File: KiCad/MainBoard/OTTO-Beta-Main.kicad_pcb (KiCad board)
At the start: 4 copper layers, 288.5 x 95 mm, 333 parts, among them J1 Conn_ARM_JTAG_SWD_10, J2 Conn_02x04, J201 Raspberry Pi Connector, J206 Conn_02x06, J207 Conn_02x03, J3 Conn_02x05, J4 Conn_02x05, J5 Conn_02x05, J6 Conn_02x05, J7 Conn_01x20, J9 Conn_01x03, Q1 AO4407A, Q2 2N7002, SW1 ALPS SKHC, SW10 ALPS SKHC, SW11 ALPS SKHC, SW12 ALPS SKHC, SW13 ALPS SKHC, SW14 ALPS SKHC, SW15 ALPS SKHC, SW16 ALPS SKHC, SW17 ALPS SKHC, SW18 ALPS SKHC, SW19 ALPS SKHC, SW2 ALPS SKHC, SW20 ALPS SKHC, SW201 5.2x5.2x1.5mm, SW202 SW_DIP_x02, SW21 ALPS SKHC, SW22 ALPS SKHC, SW23 ALPS SKHC, SW24 ALPS SKHC, SW25 ALPS SKHC, SW26 ALPS SKHC, SW27 6x6x13mm, SW28 6x6x13mm, SW29 6x6x13mm, SW3 ALPS SKHC, SW30 6x6x13mm, SW31 6x6x13mm, SW32 6x6x13mm, SW33 6x6x13mm, SW34 6x6x13mm, SW35 6x6x13mm, SW36 6x6x13mm, SW37 6x6x13mm, SW38 6x6x13mm, SW39 6x6x13mm, SW4 ALPS SKHC, SW40 6x6x13mm, SW41 6x6x13mm, SW42 6x6x13mm, SW43 6x6x13mm, SW44 6x6x13mm, SW45 6x6x13mm, SW46 6x6x13mm, SW47 6x6x13mm, SW48 SW_DIP_x02, SW49 SW_DPDT_x2, SW5 ALPS SKHC, SW50 6x6x13mm, SW51 6x6x13mm, SW52 6x6x13mm, SW53 6x6x13mm, SW54 6x6x13mm, SW55 6x6x13mm, SW56 6x6x13mm, SW6 ALPS SKHC, SW7 ALPS SKHC, SW8 ALPS SKHC, SW9 ALPS SKHC, U1 TPS5430DDA, U2 TPS54331DR, U201 6N137, U202 STM32F407VGTx, U204 SRV05-4, U205 SN74HC14, U207 WM8731, U208 AMS1117-3.3, U5 TPS22918_SOT23-6_A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

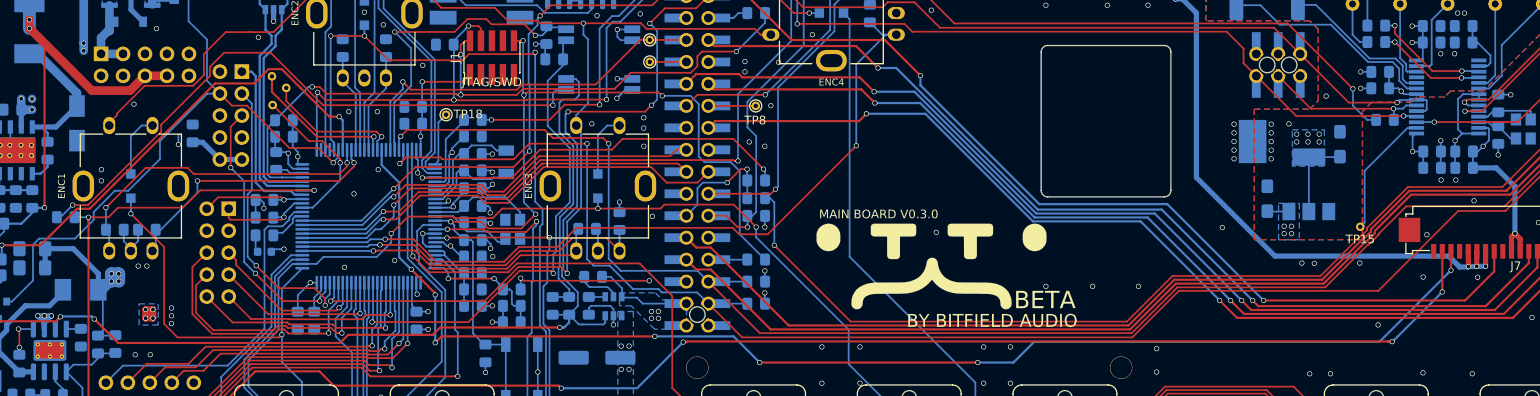
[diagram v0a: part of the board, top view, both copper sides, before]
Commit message: LEDs on PI power on main board
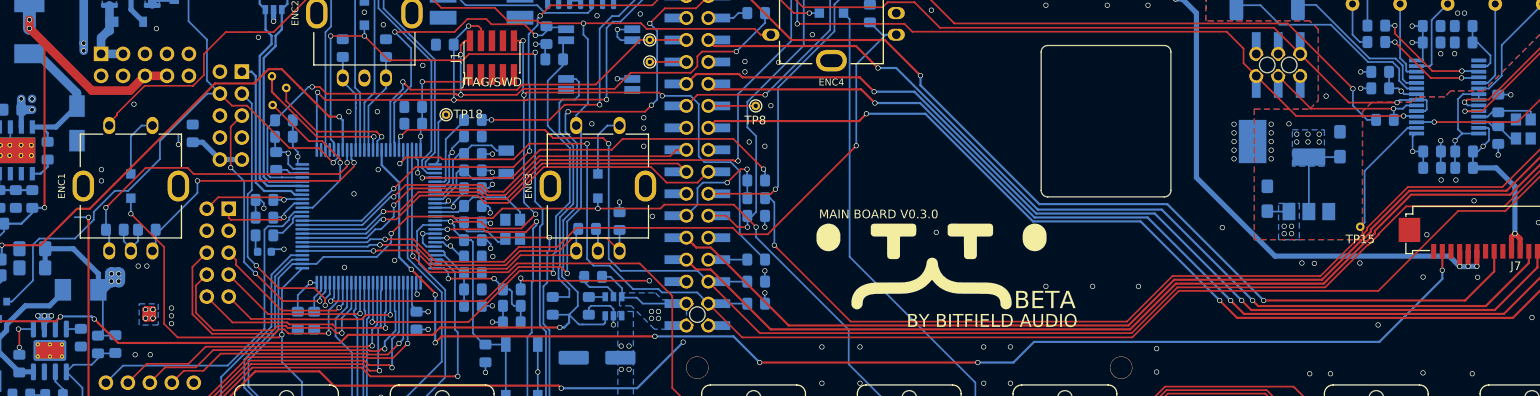
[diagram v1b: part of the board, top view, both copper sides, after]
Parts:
- removed R31, R32: 10k, Resistor_SMD:R_0805_2012Metric_Pad1.15x1.40mm_HandSolder
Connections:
- DC201 pad 3: Net-(DC201-Pad3) -> (no net)
- J1 pad 6: Net-(J1-Pad6) -> (no net)
- J1 pad 7: Net-(J1-Pad7) -> (no net)
- J1 pad 8: Net-(J1-Pad8) -> (no net)
- J4 pad 6: Net-(J4-Pad6) -> (no net)
- J7 pad 14: +5V_REG -> GND
- J7 pad 15: +5V_REG -> +5V_RASPI
- J7 pad 16: +5V_REG -> +5V_RASPI
- J7 pad 17: GND -> +5V_RASPI
- J7 pad 18: SPI_MOSI_MCU -> GND
- J7 pad 19: LED_PWR_EN -> SPI_MOSI_MCU
- SW48 pad 2: +3V3_MCU -> (no net)
- SW48 pad 3: /MCU/PERIPHERALS/LED_PWR_EN_OVERRIDE -> (no net)
- SW49 pad 3: Net-(SW49-Pad3) -> (no net)
- TRS201 pad R1S: Net-(TRS201-PadR1S) -> (no net)
- TRS201 pad R2S: Net-(TRS201-PadR2S) -> (no net)
- TRS201 pad SS: Net-(TRS201-PadSS) -> (no net)
- TRS201 pad TS: Net-(TRS201-PadTS) -> (no net)
- TRS202 pad R1S: Net-(TRS202-PadR1S) -> (no net)
- TRS202 pad R2S: Net-(TRS202-PadR2S) -> (no net)
- TRS202 pad SS: Net-(TRS202-PadSS) -> (no net)
- TRS202 pad TS: Net-(TRS202-PadTS) -> (no net)
- TRS203 pad R1S: Net-(TRS203-PadR1S) -> (no net)
- TRS203 pad R2: Net-(TRS203-PadR2) -> (no net)
- TRS203 pad R2S: Net-(TRS203-PadR2S) -> (no net)
- TRS203 pad SS: Net-(TRS203-PadSS) -> (no net)
- TRS203 pad TS: Net-(TRS203-PadTS) -> (no net)
- TRS204 pad R1S: Net-(TRS204-PadR1S) -> (no net)
- TRS204 pad SS: Net-(TRS204-PadSS) -> (no net)
- TRS204 pad TS: Net-(TRS204-PadTS) -> (no net)
- TRS205 pad R1S: Net-(TRS205-PadR1S) -> (no net)
- TRS205 pad SS: Net-(TRS205-PadSS) -> (no net)
- TRS205 pad TS: Net-(TRS205-PadTS) -> (no net)
- TRS206 pad SS: Net-(TRS206-PadSS) -> (no net)
- U1 pad 2: Net-(U1-Pad2) -> (no net)
- U1 pad 3: Net-(U1-Pad3) -> (no net)
- U1 pad 5: Net-(U1-Pad5) -> (no net)
- U201 pad 1: Net-(U201-Pad1) -> (no net)
- U201 pad 7: Net-(U201-Pad7) -> (no net)
- U202 pad 24: Net-(U202-Pad24) -> (no net)
- U202 pad 26: /MCU/MCU_PA3 -> (no net)
- U202 pad 69: LED_PWR_EN -> (no net)
- U202 pad 7: Net-(U202-Pad7) -> (no net)
- U202 pad 77: Net-(U202-Pad77) -> (no net)
- U202 pad 79: Net-(U202-Pad79) -> (no net)
- U202 pad 92: /GPIO0_RASPI -> (no net)
- U204 pad 4: Net-(U204-Pad4) -> (no net)
- U204 pad 6: Net-(U204-Pad6) -> (no net)
- U205 pad 12: Net-(U205-Pad12) -> (no net)
- U205 pad 2: Net-(U205-Pad2) -> (no net)
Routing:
- net LED_PWR_EN: track 223.7 -> 0.00 mm, vias 6 -> 0
- net (no net): track 0.00 -> 100.0 mm, vias 3 -> 6
- net /MCU/PERIPHERALS/LED_PWR_EN_OVERRIDE: track 71.9 -> 0.00 mm, vias 2 -> 0
- net +5V_REG: track 191.0 -> 122.6 mm, vias 29 -> 23
- net +5V_RASPI: track 96.9 -> 164.2 mm, vias 12 -> 18
- net +3V3_MCU: track 91.0 -> 88.8 mm, vias 18 -> 17

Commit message: Redesign for STM32F103
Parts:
- removed C221, C222: 2.2uF, Capacitor_SMD:C_0805_2012Metric_Pad1.15x1.40mm_HandSolder
- removed C56: 100nF, Capacitor_SMD:C_0805_2012Metric_Pad1.15x1.40mm_HandSolder
- removed J5, J6: Conn_02x05, Connector_PinHeader_2.54mm:PinHeader_2x05_P2.54mm_Vertical
- removed R206, R207: 2.2k, Resistor_SMD:R_0805_2012Metric_Pad1.15x1.40mm_HandSolder
- removed R235, R236, R237, R238: 33, Resistor_SMD:R_0805_2012Metric_Pad1.15x1.40mm_HandSolder
- removed R29, R30: 10k, Resistor_SMD:R_0805_2012Metric_Pad1.15x1.40mm_HandSolder
- removed TP1, TP16, TP17, TP18, TP9: TestPoint, TestPoint:TestPoint_THTPad_D1.0mm_Drill0.5mm
- added JP1: Jumper_2_Bridged, Jumper:SolderJumper-2_P1.3mm_Bridged_Pad1.0x1.5mm, B.Cu at (26.8, 26.5)
- added JP2: Jumper_2_Bridged, Jumper:SolderJumper-2_P1.3mm_Bridged_Pad1.0x1.5mm, B.Cu at (26.8, 28.5)
- R16: footprint Resistor_SMD:R_0805_2012Metric_Pad1.15x1.40mm_HandSolder -> Resistor_SMD:R_0805_2012Metric
- U2: footprint Package_SO:SOIC-8-1EP_3.9x4.9mm_P1.27mm_EP2.41x3.81mm_ThermalVias -> OTTO_Footprints_Lib:SOIC-8-1EP_3.9x4.9mm_P1.27mm_EP2.41x3.81mm_ThermalVias
- U202: value STM32F407VGTx -> STM32F103R8T6; footprint OTTO_Footprints_Lib:LQFP-100_14x14mm_P0.5mm -> OTTO_Footprints_Lib:LQFP-64_10x10mm_P0.5mm
- Y201: value 25MHz -> 16MHz
- moved J4 40.9 mm to (41.9, 78.9), turned to 90 degrees
- moved C4 17.9 mm to (26.4, 17.9), turned to 180 degrees
- moved C3 11.6 mm to (54.0, 45.9), turned to 0 degrees
- moved TP15 10.9 mm to (181.1, 46.0)
- moved R6 6.44 mm to (54.0, 50.4), turned to 0 degrees
- moved C52 4.09 mm to (57.7, 64.6), turned to 180 degrees
- moved TP8 4.00 mm to (111.5, 42.3), turned to 90 degrees
- moved D57 3.70 mm to (47.5, 57.4), turned to 180 degrees
- moved C51 3.06 mm to (66.5, 64.6), turned to 0 degrees
- moved L1 2.66 mm to (23.5, 36.0)
- moved C53 2.44 mm to (54.0, 48.1)
- moved R16 1.98 mm to (86.0, 65.5)
- moved Y201 1.97 mm to (78.8, 54.7)
- moved C5 1.36 mm to (20.9, 56.0)
- moved Q2 1.25 mm to (19.9, 64.7), turned to 90 degrees
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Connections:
- C1 pad 2: /MCU/BARREL_IN -> /MCU/BUCK_IN
- J3 pad 10: GND -> /MCU/+5V_USB
- J3 pad 2: /MCU/BARREL_IN -> /MCU/BUCK_IN
- J3 pad 4: /MCU/BARREL_IN -> /MCU/BUCK_IN
- J3 pad 6: +5V_REG -> /MCU/BUCK_OUT
- J3 pad 8: +5V_REG -> /MCU/BUCK_OUT
- J3 pad 9: GND -> /MCU/+5V_USB
- J4 pad 1: /MCU/+5V_USB -> GND
- J4 pad 2: /MCU/+5V_USB -> GND
- J4 pad 4: PWR_BUTTON -> GND
- J4 pad 6: (no net) -> PWR_BUTTON
- J7 pad 15: +5V_RASPI -> +5V_REG
- J7 pad 16: +5V_RASPI -> +5V_REG
- J7 pad 17: +5V_RASPI -> +5V_REG
- J7 pad 20: GND -> LED_PWR_EN
- L1 pad 2: +5V_REG -> /MCU/BUCK_OUT
- R14 pad 1: +5V_REG -> /MCU/BUCK_OUT
- SW48 pad 2: (no net) -> +3V3_MCU
- SW48 pad 3: (no net) -> LED_PWR_EN
- U1 pad 7: /MCU/BARREL_IN -> /MCU/BUCK_IN
- U202 pad 1: (F427)_SAI1_MCLK_A -> +3V3_MCU
- U202 pad 10: GND -> TRIGGER2
- U202 pad 11: +3V3_MCU -> TRIGGER3
- U202 pad 12: /MCU/OSC_IN -> GND
- U202 pad 13: /MCU/OSC_OUT -> +3V3A_MCU
- U202 pad 14: /ICP_RST -> /MCU/ENC_B_3
- U202 pad 15: /MCU/ROW_5 -> /MCU/ENC_A_3
- U202 pad 16: /MCU/ROW_6 -> MIDI_OUT
- U202 pad 17: GND -> MIDI_IN
- U202 pad 18: /MCU/ROW_8 -> GND
- U202 pad 2: (F427)_SAI1_SD_B -> /PWM1_GPIO13_RASPI
- U202 pad 21: +3V3A_MCU -> (no net)
- U202 pad 22: +3V3A_MCU -> /MCU/COL_3
- U202 pad 23: /MCU/MCU_PA0 -> SPI_MOSI_MCU
- U202 pad 24: (no net) -> /MCU/COL_4
- U202 pad 25: /MCU/3V3_RASPI_DIV_2 -> /MCU/COL_5
- U202 pad 26: (no net) -> /MCU/COL_2
- U202 pad 27: GND -> /MCU/COL_7
- U202 pad 28: +3V3_MCU -> /MCU/BOOT1
- U202 pad 29: /MCU/CV_DAC_1 -> /MCU/COL_6
- U202 pad 3: (F427)_SAI1_FS_A -> /MCU/OSC32_IN
- U202 pad 30: /MCU/CV_DAC_2 -> /MCU/COL_1
- U202 pad 31: /MCU/CV_ADC_1 -> GND
- U202 pad 32: /MCU/CV_ADC_2 -> +3V3_MCU
- U202 pad 33: /MCU/EXP_GPIO_1_ADC -> /MCU/ROW_2
- U202 pad 34: /MCU/EXP_GPIO_2_ADC -> /MCU/ROW_3
- U202 pad 35: /MCU/GATE_IO_1 -> /MCU/ROW_4
- U202 pad 36: /MCU/GATE_IO_2 -> /MCU/ROW_5
- U202 pad 37: /MCU/BOOT1 -> /MCU/STATUS_LED
- U202 pad 38: /MCU/COL_3 -> /MCU/ENC_B_1
- U202 pad 39: /MCU/COL_4 -> /MCU/ENC_A_1
- U202 pad 4: (F427)_SAI1_SCK_A -> /MCU/OSC32_OUT
- U202 pad 40: /MCU/EXP_GPIO_3_PWM -> /MCU/ROW_1
- U202 pad 41: /MCU/COL_5 -> LED_PWR_EN
- U202 pad 42: /MCU/EXP_GPIO_4_PWM -> /MCU/PROG_UART_TX
- U202 pad 43: /MCU/COL_6 -> /MCU/PROG_UART_RX
- U202 pad 44: /MCU/EXP_GPIO_5_PWM -> /MCU/USBD_N
- U202 pad 45: /MCU/EXP_GPIO_6_PWM -> /MCU/USBD_P
- U202 pad 46: /MCU/COL_7 -> /ICP_SWDIO
- U202 pad 47: /MCU/PROG_UART_TX -> GND
- U202 pad 48: /MCU/PROG_UART_RX -> +3V3_MCU
- U202 pad 49: Net-(C221-Pad1) -> /ICP_SWCLK
- U202 pad 5: (F427)_SAI1_SD_A -> /MCU/OSC_IN
- U202 pad 50: +3V3_MCU -> /MCU/ENC_B_4
- U202 pad 51: /MCU/ROW_1 -> PWR_HOLD
- U202 pad 52: /MCU/ROW_2 -> PWR_BUTTON
- U202 pad 53: /MCU/ROW_3 -> /MCU/ENC_A_2
- U202 pad 54: /MCU/ROW_4 -> /GPIO1_RASPI
- U202 pad 55: /MCU/ENC_A_3 -> /MCU/COL_8
- U202 pad 56: /MCU/ENC_B_3 -> /MCU/ROW_7
- U202 pad 57: /MCU/ENC_A_4 -> /MCU/ENC_B_2
- U202 pad 58: /MCU/ENC_B_4 -> I2C_SCL
- U202 pad 59: TRIGGER1 -> I2C_SDA
- U202 pad 6: +3V3_MCU -> /MCU/OSC_OUT
- U202 pad 60: TRIGGER2 -> /MCU/BOOT0
- U202 pad 61: TRIGGER3 -> /MCU/ROW_6
- U202 pad 62: /PWM1_GPIO13_RASPI -> /MCU/ROW_8
- U202 pad 63: /MCU/STATUS_LED -> GND
- U202 pad 64: /MCU/MCU_PC7 -> +3V3_MCU
- U202 pad 7: (no net) -> /ICP_RST
- U202 pad 8: /MCU/OSC32_IN -> /MCU/ENC_A_4
- U202 pad 9: /MCU/OSC32_OUT -> TRIGGER1
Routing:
- net LED_PWR_EN: track 0.00 -> 163.5 mm, vias 0 -> 2
- net (no net): track 100.0 -> 0.00 mm, vias 6 -> 3
- net (F427)_SAI1_SD_B: track 85.5 -> 0.00 mm, vias 2 -> 0
- net (F427)_SAI1_FS_A: track 85.0 -> 0.00 mm, vias 2 -> 0
- net +5V_RASPI: track 164.2 -> 94.7 mm, vias 18 -> 12
- net /MCU/MCU_PA0: track 61.1 -> 0.00 mm, vias 1 -> 0
- net /MCU/BUCK_OUT: track 0.00 -> 51.2 mm
- net /MCU/BARREL_IN: track 65.0 -> 15.2 mm, vias 6 -> 0
- net (F427)_SAI1_SCK_A: track 45.6 -> 0.00 mm, vias 2 -> 0
- net /MCU/GATE_IO_1: track 44.6 -> 0.00 mm, vias 1 -> 0
- net /MCU/CV_ADC_1: track 43.1 -> 0.00 mm, vias 1 -> 0
- net /MCU/CV_DAC_1: track 39.4 -> 0.00 mm, vias 1 -> 0
- net /MCU/BUCK_IN: track 0.00 -> 39.3 mm, vias 0 -> 7
- net I2S_DIN: track 131.2 -> 92.7 mm, vias 3 -> 1
- net /MCU/MCU_PC7: track 37.8 -> 0.00 mm
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- added copper zone on B.Cu, net +3V3_MCU
- added copper zone on B.Cu, net /MCU/BUCK_IN
- added copper zone on In1.Cu, net /MCU/BUCK_IN
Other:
- board text added: "Cut when installing battery board"
